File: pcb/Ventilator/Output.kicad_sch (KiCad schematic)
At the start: 16 parts, among them J3 Screw_Terminal_01x08, K1 FINDER-40.52.7.012.0000, K2 FINDER-40.52.7.012.0000, K3 FINDER-40.52.7.012.0000, Q1 NUD3160, Q2 NUD3160, Q3 NUD3160

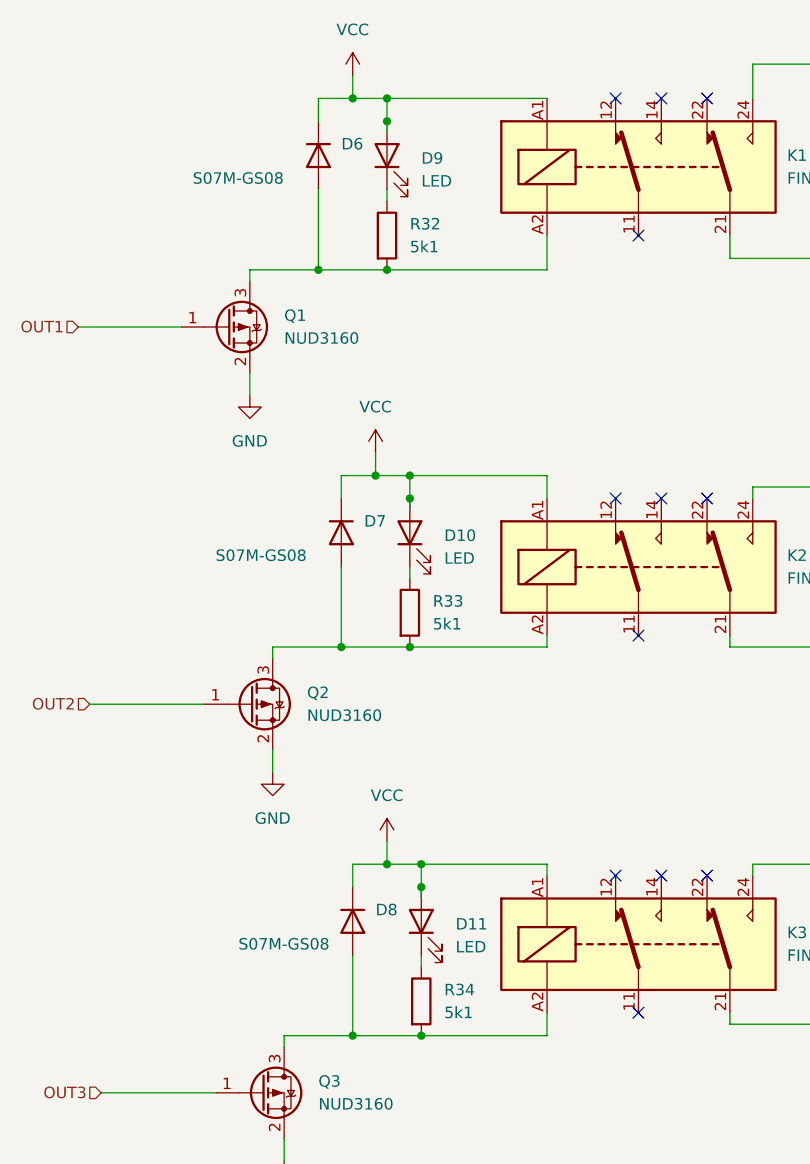
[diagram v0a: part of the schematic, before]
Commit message: - all parts connected, placed partially
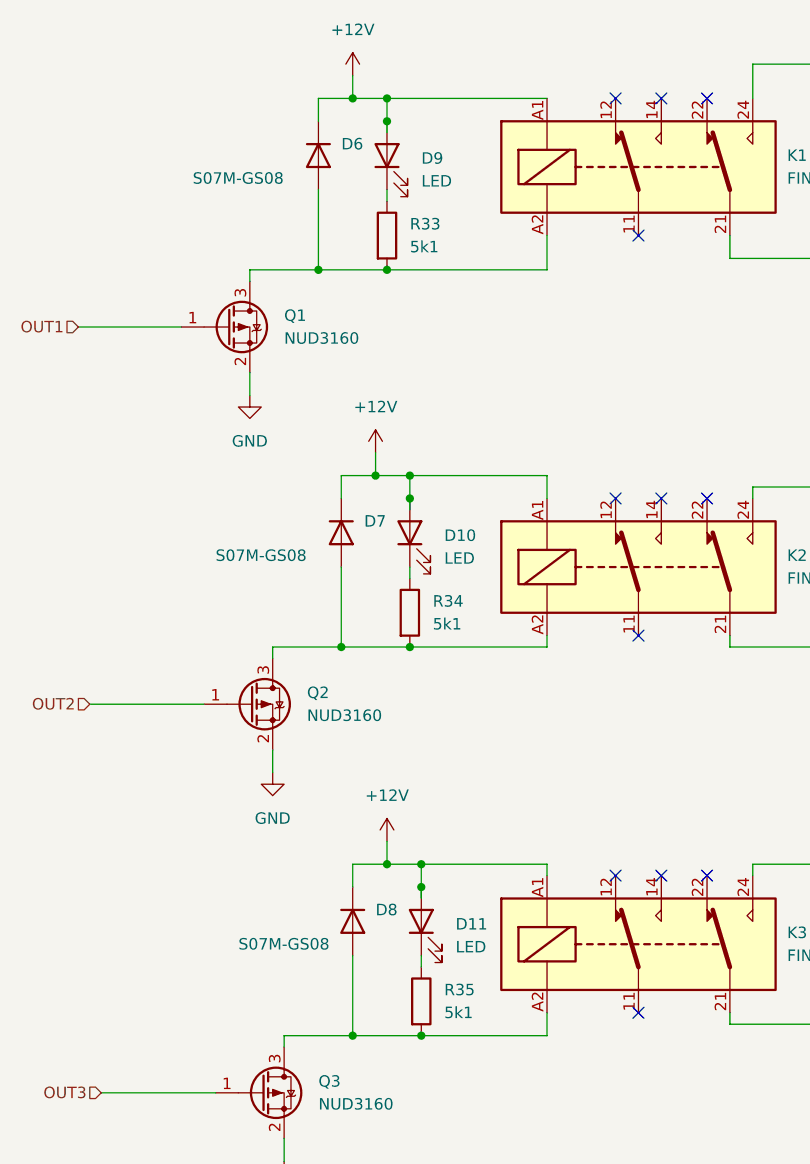
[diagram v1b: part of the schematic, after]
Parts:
- renumbered R32 to R33, R33 to R34, R34 to R35
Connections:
- net VCC renamed +12V
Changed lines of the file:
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@@
     (effects (font (size 1.27 1.27)) (justify right))
+  )
+  (symbol (lib_id "power:+12V") (at 110.49 123.19 0) (unit 1)
+    (in_bom yes) (on_board yes) (fields_autoplaced)
+    (property "Reference" "#PWR0105" (id 0) (at 110.49 127 0)
+      (effects (font (size 1.27 1.27)) hide)
+    )
+    (property "Value" "+12V" (id 1) (at 110.49 118.11 0))
+    (property "Footprint" "" (id 2) (at 110.49 123.19 0)
+      (effects (font (size 1.27 1.27)) hide)
+    )
+    (property "Datasheet" "" (id 3) (at 110.49 123.19 0)
+      (effects (font (size 1.27 1.27)) hide)
+    )
+    (pin "1")
   )
   (symbol (lib_id "Device:D") (at 102.87 46.99 270) (unit 1)
@@
     (pin "3")
   )
-  (symbol (lib_id "power:VCC") (at 106.68 38.1 0) (unit 1)
-    (in_bom yes) (on_board yes) (fields_autoplaced)
-    (property "Reference" "#PWR023" (id 0) (at 106.68 41.91 0)
-      (effects (font (size 1.27 1.27)) hide)
-    )
-    (property "Value" "VCC" (id 1) (at 106.68 33.02 0))
-    (property "Footprint" "" (id 2) (at 106.68 38.1 0)
-      (effects (font (size 1.27 1.27)) hide)
-    )
-    (property "Datasheet" "" (id 3) (at 106.68 38.1 0)
-      (effects (font (size 1.27 1.27)) hide)
-    )
-    (pin "1")
-  )
   (symbol (lib_id "Device:R") (at 114.3 140.97 0) (unit 1)
     (in_bom yes) (on_board yes) (fields_autoplaced)
-    (property "Reference" "R34" (id 0) (at 116.84 139.6999 0)
+    (property "Reference" "R35" (id 0) (at 116.84 139.6999 0)
       (effects (font (size 1.27 1.27)) (justify left))
     )
@@
   (symbol (lib_id "Device:R") (at 110.49 55.88 0) (unit 1)
     (in_bom yes) (on_board yes) (fields_autoplaced)
-    (property "Reference" "R32" (id 0) (at 113.03 54.6099 0)
+    (property "Reference" "R33" (id 0) (at 113.03 54.6099 0)
       (effects (font (size 1.27 1.27)) (justify left))
     )
@@
   (symbol (lib_id "Device:R") (at 113.03 97.79 0) (unit 1)
     (in_bom yes) (on_board yes) (fields_autoplaced)
-    (property "Reference" "R33" (id 0) (at 115.57 96.5199 0)
+    (property "Reference" "R34" (id 0) (at 115.57 96.5199 0)
       (effects (font (size 1.27 1.27)) (justify left))
     )
@@
     (pin "2")
   )
-  (symbol (lib_id "power:VCC") (at 109.22 80.01 0) (unit 1)
-    (in_bom yes) (on_board yes) (fields_autoplaced)
-    (property "Reference" "#PWR024" (id 0) (at 109.22 83.82 0)
-      (effects (font (size 1.27 1.27)) hide)
-    )
-    (property "Value" "VCC" (id 1) (at 109.22 74.93 0))
-    (property "Footprint" "" (id 2) (at 109.22 80.01 0)
-      (effects (font (size 1.27 1.27)) hide)
-    )
-    (property "Datasheet" "" (id 3) (at 109.22 80.01 0)
-      (effects (font (size 1.27 1.27)) hide)
-    )
-    (pin "1")
-  )
   (symbol (lib_id "power:GND") (at 97.79 115.57 0) (unit 1)
     (in_bom yes) (on_board yes) (fields_autoplaced)
-    (property "Reference" "#PWR021" (id 0) (at 97.79 121.92 0)
+    (property "Reference" "#PWR023" (id 0) (at 97.79 121.92 0)
       (effects (font (size 1.27 1.27)) hide)
     )
@@
   (symbol (lib_id "power:GND") (at 99.06 158.75 0) (unit 1)
     (in_bom yes) (on_board yes) (fields_autoplaced)
-    (property "Reference" "#PWR022" (id 0) (at 99.06 165.1 0)
+    (property "Reference" "#PWR024" (id 0) (at 99.06 165.1 0)
       (effects (font (size 1.27 1.27)) hide)
     )
@@
     (pin "2")
   )
+  (symbol (lib_id "power:+12V") (at 109.22 80.01 0) (unit 1)
+    (in_bom yes) (on_board yes) (fields_autoplaced)
+    (property "Reference" "#PWR0103" (id 0) (at 109.22 83.82 0)
+      (effects (font (size 1.27 1.27)) hide)
+    )
+    (property "Value" "+12V" (id 1) (at 109.22 74.93 0))
+    (property "Footprint" "" (id 2) (at 109.22 80.01 0)
+      (effects (font (size 1.27 1.27)) hide)
+    )
+    (property "Datasheet" "" (id 3) (at 109.22 80.01 0)
+      (effects (font (size 1.27 1.27)) hide)
+    )
+    (pin "1")
+  )
   (symbol (lib_id "power:GND") (at 95.25 73.66 0) (unit 1)
     (in_bom yes) (on_board yes) (fields_autoplaced)
-    (property "Reference" "#PWR020" (id 0) (at 95.25 80.01 0)
+    (property "Reference" "#PWR022" (id 0) (at 95.25 80.01 0)
       (effects (font (size 1.27 1.27)) hide)
     )
@@
     )
     (property "Datasheet" "" (id 3) (at 95.25 73.66 0)
-      (effects (font (size 1.27 1.27)) hide)
-    )
-    (pin "1")
-  )
-  (symbol (lib_id "power:VCC") (at 110.49 123.19 0) (unit 1)
-    (in_bom yes) (on_board yes) (fields_autoplaced)
-    (property "Reference" "#PWR025" (id 0) (at 110.49 127 0)
-      (effects (font (size 1.27 1.27)) hide)
-    )
-    (property "Value" "VCC" (id 1) (at 110.49 118.11 0))
-    (property "Footprint" "" (id 2) (at 110.49 123.19 0)
-      (effects (font (size 1.27 1.27)) hide)
-    )
-    (property "Datasheet" "" (id 3) (at 110.49 123.19 0)
       (effects (font (size 1.27 1.27)) hide)
     )
@@
     (pin "3")
   )
+  (symbol (lib_id "power:+12V") (at 106.68 38.1 0) (unit 1)
+    (in_bom yes) (on_board yes) (fields_autoplaced)
+    (property "Reference" "#PWR0104" (id 0) (at 106.68 41.91 0)
+      (effects (font (size 1.27 1.27)) hide)
+    )
+    (property "Value" "+12V" (id 1) (at 106.68 33.02 0))
+    (property "Footprint" "" (id 2) (at 106.68 38.1 0)
+      (effects (font (size 1.27 1.27)) hide)
+    )
+    (property "Datasheet" "" (id 3) (at 106.68 38.1 0)
+      (effects (font (size 1.27 1.27)) hide)
+    )
+    (pin "1")
+  )
   (symbol (lib_id "Relay:FINDER-40.52") (at 138.43 92.71 0) (unit 1)

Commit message: - voor autorouter
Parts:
- renumbered R33 to R32, R34 to R33, R35 to R34
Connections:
- net at K3.11: now also J3.6 (Pin_6), K3.21
- net at K3.14: now also J3.5 (Pin_5), K3.24
- net at K1.11: now also J3.2 (Pin_2), K1.21
- net at K1.14: now also J3.1 (Pin_1), K1.24
- net at J3.3 (Pin_3), K2.24: now also K2.14
- net at J3.4 (Pin_4), K2.21: now also K2.11
- no-connect marks 14 -> 8
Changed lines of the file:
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@@
   (junction (at 110.49 40.64) (diameter 0) (color 0 0 0 0)
   )
+  (junction (at 148.59 58.42) (diameter 0) (color 0 0 0 0)
+  )
+  (junction (at 151.13 125.73) (diameter 0) (color 0 0 0 0)
+  )
   (junction (at 114.3 128.27) (diameter 0) (color 0 0 0 0)
   )
+  (junction (at 148.59 101.6) (diameter 0) (color 0 0 0 0)
+  )
   (junction (at 105.41 101.6) (diameter 0) (color 0 0 0 0)
   )
@@
   (junction (at 110.49 59.69) (diameter 0) (color 0 0 0 0)
   )
+  (junction (at 148.59 143.51) (diameter 0) (color 0 0 0 0)
+  )
   (junction (at 113.03 82.55) (diameter 0) (color 0 0 0 0)
   )
   (junction (at 113.03 101.6) (diameter 0) (color 0 0 0 0)
   )
+  (junction (at 151.13 36.83) (diameter 0) (color 0 0 0 0)
+  )
   (junction (at 110.49 43.18) (diameter 0) (color 0 0 0 0)
   )
@@
   )
   (junction (at 106.68 144.78) (diameter 0) (color 0 0 0 0)
+  )
+  (junction (at 151.13 83.82) (diameter 0) (color 0 0 0 0)
   )
   (junction (at 102.87 59.69) (diameter 0) (color 0 0 0 0)
@@
   (no_connect (at 207.01 100.33))
   (no_connect (at 146.05 127))
-  (no_connect (at 138.43 142.24))
   (no_connect (at 135.89 85.09))
-  (no_connect (at 138.43 100.33))
-  (no_connect (at 138.43 55.88))
-  (no_connect (at 140.97 85.09))
-  (no_connect (at 140.97 40.64))
   (no_connect (at 207.01 97.79))
   (no_connect (at 135.89 40.64))
-  (no_connect (at 140.97 127))
   (no_connect (at 135.89 127))
   (wire (pts (xy 102.87 43.18) (xy 102.87 40.64))
@@
     (stroke (width 0) (type default) (color 0 0 0 0))
   )
+  (wire (pts (xy 138.43 100.33) (xy 138.43 101.6))
+    (stroke (width 0) (type default) (color 0 0 0 0))
+  )
   (wire (pts (xy 105.41 101.6) (xy 97.79 101.6))
     (stroke (width 0) (type default) (color 0 0 0 0))
@@
     (stroke (width 0) (type default) (color 0 0 0 0))
   )
+  (wire (pts (xy 138.43 143.51) (xy 148.59 143.51))
+    (stroke (width 0) (type default) (color 0 0 0 0))
+  )
   (wire (pts (xy 196.85 101.6) (xy 196.85 90.17))
     (stroke (width 0) (type default) (color 0 0 0 0))
@@
     (stroke (width 0) (type default) (color 0 0 0 0))
   )
+  (wire (pts (xy 140.97 36.83) (xy 151.13 36.83))
+    (stroke (width 0) (type default) (color 0 0 0 0))
+  )
   (wire (pts (xy 95.25 71.12) (xy 95.25 73.66))
     (stroke (width 0) (type default) (color 0 0 0 0))
@@
     (stroke (width 0) (type default) (color 0 0 0 0))
   )
+  (wire (pts (xy 138.43 55.88) (xy 138.43 58.42))
+    (stroke (width 0) (type default) (color 0 0 0 0))
+  )
   (wire (pts (xy 148.59 58.42) (xy 200.66 58.42))
     (stroke (width 0) (type default) (color 0 0 0 0))
@@
     (stroke (width 0) (type default) (color 0 0 0 0))
   )
+  (wire (pts (xy 140.97 83.82) (xy 151.13 83.82))
+    (stroke (width 0) (type default) (color 0 0 0 0))
+  )
   (wire (pts (xy 110.49 59.69) (xy 102.87 59.69))
     (stroke (width 0) (type default) (color 0 0 0 0))
@@
     (stroke (width 0) (type default) (color 0 0 0 0))
   )
+  (wire (pts (xy 140.97 125.73) (xy 151.13 125.73))
+    (stroke (width 0) (type default) (color 0 0 0 0))
+  )
   (wire (pts (xy 114.3 144.78) (xy 106.68 144.78))
     (stroke (width 0) (type default) (color 0 0 0 0))
@@
     (stroke (width 0) (type default) (color 0 0 0 0))
   )
+  (wire (pts (xy 140.97 127) (xy 140.97 125.73))
+    (stroke (width 0) (type default) (color 0 0 0 0))
+  )
   (wire (pts (xy 151.13 125.73) (xy 151.13 127))
     (stroke (width 0) (type default) (color 0 0 0 0))
@@
     (stroke (width 0) (type default) (color 0 0 0 0))
   )
+  (wire (pts (xy 138.43 101.6) (xy 148.59 101.6))
+    (stroke (width 0) (type default) (color 0 0 0 0))
+  )
   (wire (pts (xy 97.79 101.6) (xy 97.79 102.87))
     (stroke (width 0) (type default) (color 0 0 0 0))
@@
     (stroke (width 0) (type default) (color 0 0 0 0))
   )
+  (wire (pts (xy 140.97 40.64) (xy 140.97 36.83))
+    (stroke (width 0) (type default) (color 0 0 0 0))
+  )
   (wire (pts (xy 110.49 123.19) (xy 110.49 125.73))
     (stroke (width 0) (type default) (color 0 0 0 0))
@@
     (stroke (width 0) (type default) (color 0 0 0 0))
   )
+  (wire (pts (xy 138.43 58.42) (xy 148.59 58.42))
+    (stroke (width 0) (type default) (color 0 0 0 0))
+  )
   (wire (pts (xy 106.68 38.1) (xy 106.68 40.64))
     (stroke (width 0) (type default) (color 0 0 0 0))
@@
     (stroke (width 0) (type default) (color 0 0 0 0))
   )
+  (wire (pts (xy 138.43 142.24) (xy 138.43 143.51))
+    (stroke (width 0) (type default) (color 0 0 0 0))
+  )
   (wire (pts (xy 106.68 135.89) (xy 106.68 144.78))
     (stroke (width 0) (type default) (color 0 0 0 0))
@@
   )
   (wire (pts (xy 113.03 92.71) (xy 113.03 93.98))
+    (stroke (width 0) (type default) (color 0 0 0 0))
+  )
+  (wire (pts (xy 140.97 85.09) (xy 140.97 83.82))
     (stroke (width 0) (type default) (color 0 0 0 0))
   )
@@
   (symbol (lib_id "power:+12V") (at 110.49 123.19 0) (unit 1)
     (in_bom yes) (on_board yes) (fields_autoplaced)
-    (property "Reference" "#PWR030" (id 0) (at 110.49 127 0)
+    (property "Reference" "#PWR032" (id 0) (at 110.49 127 0)
       (effects (font (size 1.27 1.27)) hide)
     )
@@
   (symbol (lib_id "Device:R") (at 114.3 140.97 0) (unit 1)
     (in_bom yes) (on_board yes) (fields_autoplaced)
-    (property "Reference" "R35" (id 0) (at 116.84 139.6999 0)
+    (property "Reference" "R34" (id 0) (at 116.84 139.6999 0)
       (effects (font (size 1.27 1.27)) (justify left))
     )
@@
   (symbol (lib_id "Device:R") (at 110.49 55.88 0) (unit 1)
     (in_bom yes) (on_board yes) (fields_autoplaced)
-    (property "Reference" "R33" (id 0) (at 113.03 54.6099 0)
+    (property "Reference" "R32" (id 0) (at 113.03 54.6099 0)
       (effects (font (size 1.27 1.27)) (justify left))
     )
@@
   (symbol (lib_id "Device:R") (at 113.03 97.79 0) (unit 1)
     (in_bom yes) (on_board yes) (fields_autoplaced)
-    (property "Reference" "R34" (id 0) (at 115.57 96.5199 0)
+    (property "Reference" "R33" (id 0) (at 115.57 96.5199 0)
       (effects (font (size 1.27 1.27)) (justify left))
     )
@@
   (symbol (lib_id "power:GND") (at 97.79 115.57 0) (unit 1)
     (in_bom yes) (on_board yes) (fields_autoplaced)
-    (property "Reference" "#PWR026" (id 0) (at 97.79 121.92 0)
+    (property "Reference" "#PWR028" (id 0) (at 97.79 121.92 0)
       (effects (font (size 1.27 1.27)) hide)
     )
@@
   (symbol (lib_id "power:GND") (at 99.06 158.75 0) (unit 1)
     (in_bom yes) (on_board yes) (fields_autoplaced)
-    (property "Reference" "#PWR027" (id 0) (at 99.06 165.1 0)
+    (property "Reference" "#PWR029" (id 0) (at 99.06 165.1 0)
       (effects (font (size 1.27 1.27)) hide)
     )
@@
   (symbol (lib_id "power:+12V") (at 109.22 80.01 0) (unit 1)
     (in_bom yes) (on_board yes) (fields_autoplaced)
-    (property "Reference" "#PWR029" (id 0) (at 109.22 83.82 0)
+    (property "Reference" "#PWR031" (id 0) (at 109.22 83.82 0)
       (effects (font (size 1.27 1.27)) hide)
     )
@@
   (symbol (lib_id "power:GND") (at 95.25 73.66 0) (unit 1)
     (in_bom yes) (on_board yes) (fields_autoplaced)
-    (property "Reference" "#PWR025" (id 0) (at 95.25 80.01 0)
+    (property "Reference" "#PWR027" (id 0) (at 95.25 80.01 0)
       (effects (font (size 1.27 1.27)) hide)
     )
@@
   (symbol (lib_id "power:+12V") (at 106.68 38.1 0) (unit 1)
     (in_bom yes) (on_board yes) (fields_autoplaced)
-    (property "Reference" "#PWR028" (id 0) (at 106.68 41.91 0)
-      (effects (font (size 1.27 1.27)) hide)
-    )
+    (property "Reference" "#PWR030" (id 0) (at 106.68 41.91 0)
+      (effects (font (size 1.27 1.27)) hide)
+    )

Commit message: - as ordered (30/12/2022)
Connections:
- net 220_6: now reaches J3.6 (Pin_6), K3.11, K3.21
- net 220_5: now reaches J3.5 (Pin_5), K3.14, K3.24
- net 220_2: now reaches J3.2 (Pin_2), K1.11, K1.21
- net 220_1: now reaches J3.1 (Pin_1), K1.14, K1.24
- net 220_3: now reaches J3.3 (Pin_3), K2.14, K2.24
- net 220_4: now reaches J3.4 (Pin_4), K2.11, K2.21
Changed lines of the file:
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@@
     (stroke (width 0) (type default) (color 0 0 0 0))
+  )
+  (label "220_1" (at 181.61 36.83 0)
+    (effects (font (size 1.27 1.27)) (justify left bottom))
+  )
+  (label "220_6" (at 181.61 143.51 0)
+    (effects (font (size 1.27 1.27)) (justify left bottom))
+  )
+  (label "220_3" (at 180.34 83.82 0)
+    (effects (font (size 1.27 1.27)) (justify left bottom))
+  )
+  (label "220_4" (at 180.34 101.6 0)
+    (effects (font (size 1.27 1.27)) (justify left bottom))
+  )
+  (label "220_5" (at 181.61 125.73 0)
+    (effects (font (size 1.27 1.27)) (justify left bottom))
+  )
+  (label "220_2" (at 180.34 58.42 0)
+    (effects (font (size 1.27 1.27)) (justify left bottom))
   )
   (hierarchical_label "OUT3" (shape input) (at 78.74 151.13 180)
